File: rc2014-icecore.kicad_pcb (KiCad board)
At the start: 2 copper layers, 70.3 x 60.7 mm, 7 parts, among them J1 Conn_02x25_Odd_Even, J2 Conn_02x15_Odd_Even, J3 Conn_02x13_Odd_Even

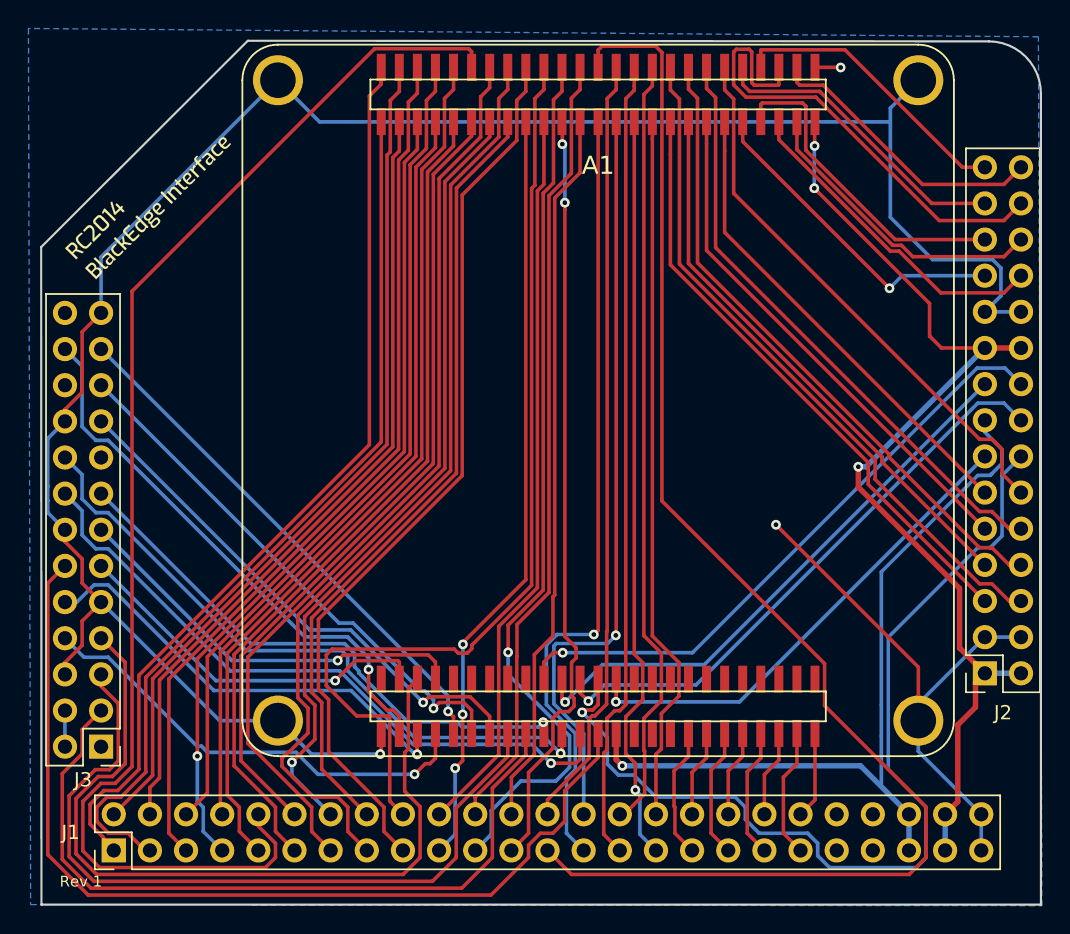
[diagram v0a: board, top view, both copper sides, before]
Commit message: Update to Kicad 6
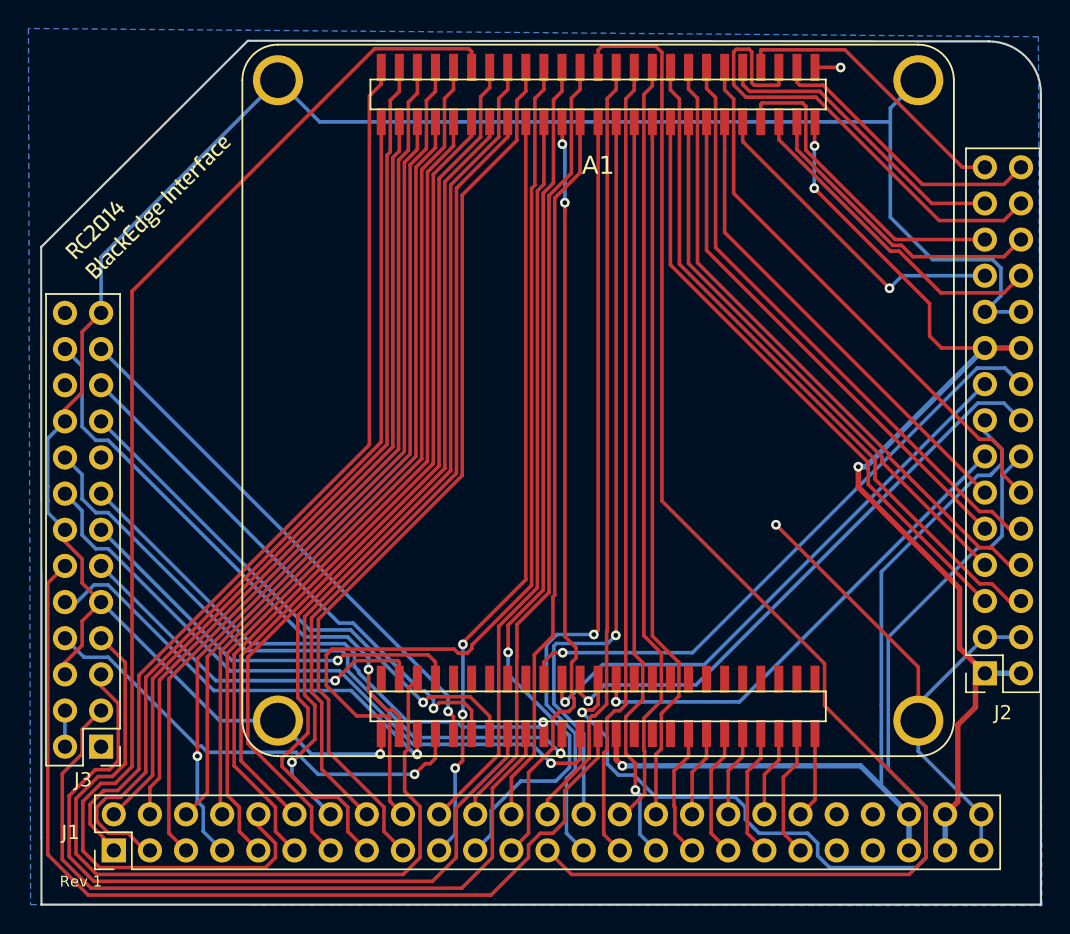
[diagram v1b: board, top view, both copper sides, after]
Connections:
- net /~ESS renamed /~{ESS}
- net /~RESET renamed /~{RESET}
- A1 pad 51: (no net) -> unconnected-(A1-Pad51)
- A1 pad 55: (no net) -> unconnected-(A1-Pad55)
- A1 pad 56: (no net) -> unconnected-(A1-Pad56)
- A1 pad 57: (no net) -> unconnected-(A1-Pad57)
- A1 pad 58: (no net) -> unconnected-(A1-Pad58)
- A1 pad 59: (no net) -> unconnected-(A1-Pad59)
- A1 pad 65: (no net) -> unconnected-(A1-Pad65)
- A1 pad 66: (no net) -> unconnected-(A1-Pad66)
- A1 pad 67: (no net) -> unconnected-(A1-Pad67)
- A1 pad 68: (no net) -> unconnected-(A1-Pad68)
- A1 pad 69: (no net) -> unconnected-(A1-Pad69)
- A1 pad 70: (no net) -> unconnected-(A1-Pad70)
- A1 pad 71: (no net) -> unconnected-(A1-Pad71)
- A1 pad 72: (no net) -> unconnected-(A1-Pad72)
- A1 pad 73: (no net) -> unconnected-(A1-Pad73)
- A1 pad 74: (no net) -> unconnected-(A1-Pad74)
- A1 pad 75: (no net) -> unconnected-(A1-Pad75)
- A1 pad 90: (no net) -> unconnected-(A1-Pad90)
- A1 pad 91: (no net) -> unconnected-(A1-Pad91)
- A1 pad 92: (no net) -> unconnected-(A1-Pad92)
- J1 pad 41: (no net) -> unconnected-(J1-Pad41)
- J1 pad 42: (no net) -> unconnected-(J1-Pad42)
- J1 pad 43: (no net) -> unconnected-(J1-Pad43)
- J1 pad 44: (no net) -> unconnected-(J1-Pad44)
- J3 pad 1: (no net) -> unconnected-(J3-Pad1)
- J3 pad 17: (no net) -> unconnected-(J3-Pad17)
- J3 pad 22: (no net) -> unconnected-(J3-Pad22)
- J3 pad 26: (no net) -> unconnected-(J3-Pad26)
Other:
- net class Default removed
- net class IO removed
- net class Power removed
